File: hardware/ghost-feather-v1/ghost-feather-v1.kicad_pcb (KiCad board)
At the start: 4 copper layers, 106.6 x 106.7 mm, 96 parts, among them J1 Conn_ARM_SWD_TagConnect_TC2030, J2 USB_C_Receptacle_USB2.0, J3 Conn_01x03, J4 Conn_01x03, J5 Conn_01x03, J6 Conn_01x03, J7 Conn_01x08, J8 Conn_01x02, Q1 BSS138, Q2 BSS138, Q3 BSS138, Q4 BSS138, SW2 BOOT0, U1 STM32F722RETx, U2 BMI270, U3 USBLC6-2SC6_MOD, U4 MPM3610, U5 MPM3610, X1 16MHz, X2 32kHz768

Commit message: feat: Via stiching #2
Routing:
- net GND: vias 329 -> 816

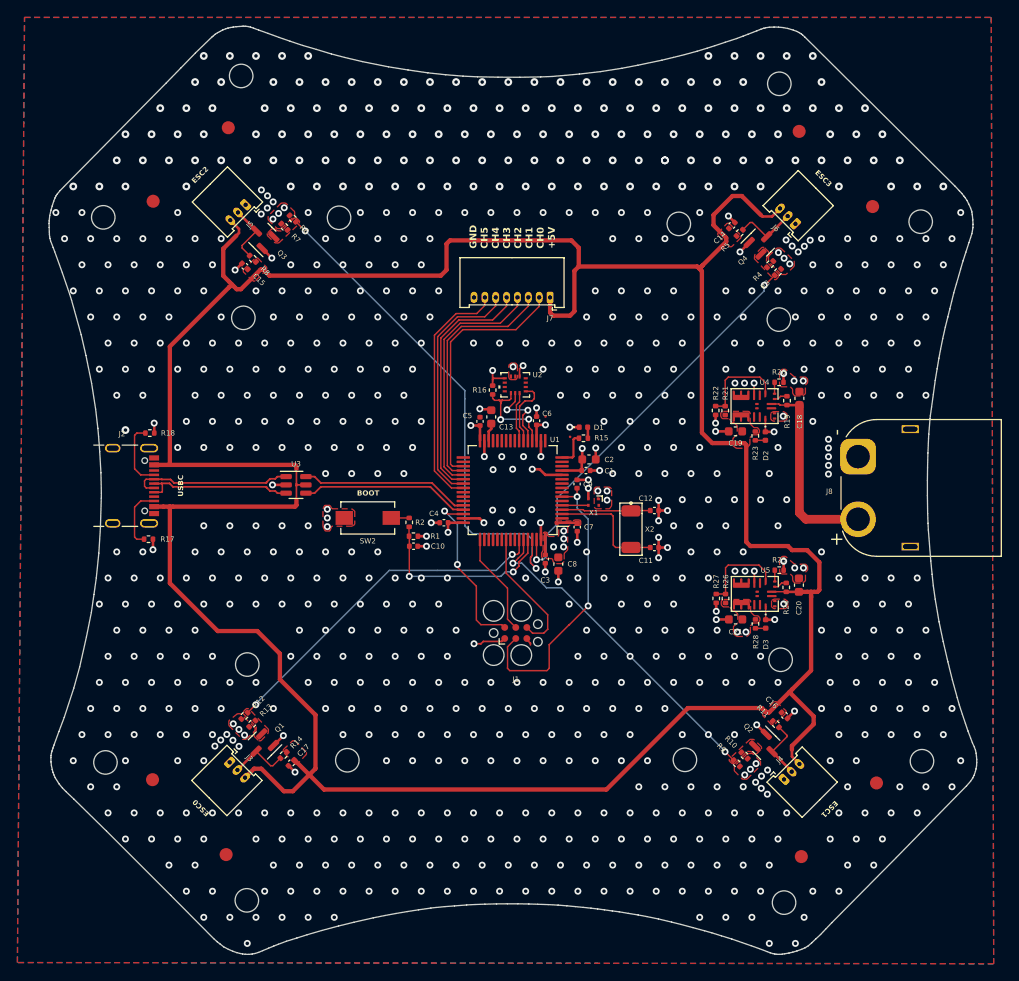
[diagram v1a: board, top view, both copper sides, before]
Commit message: feat: Remove errors and warnings
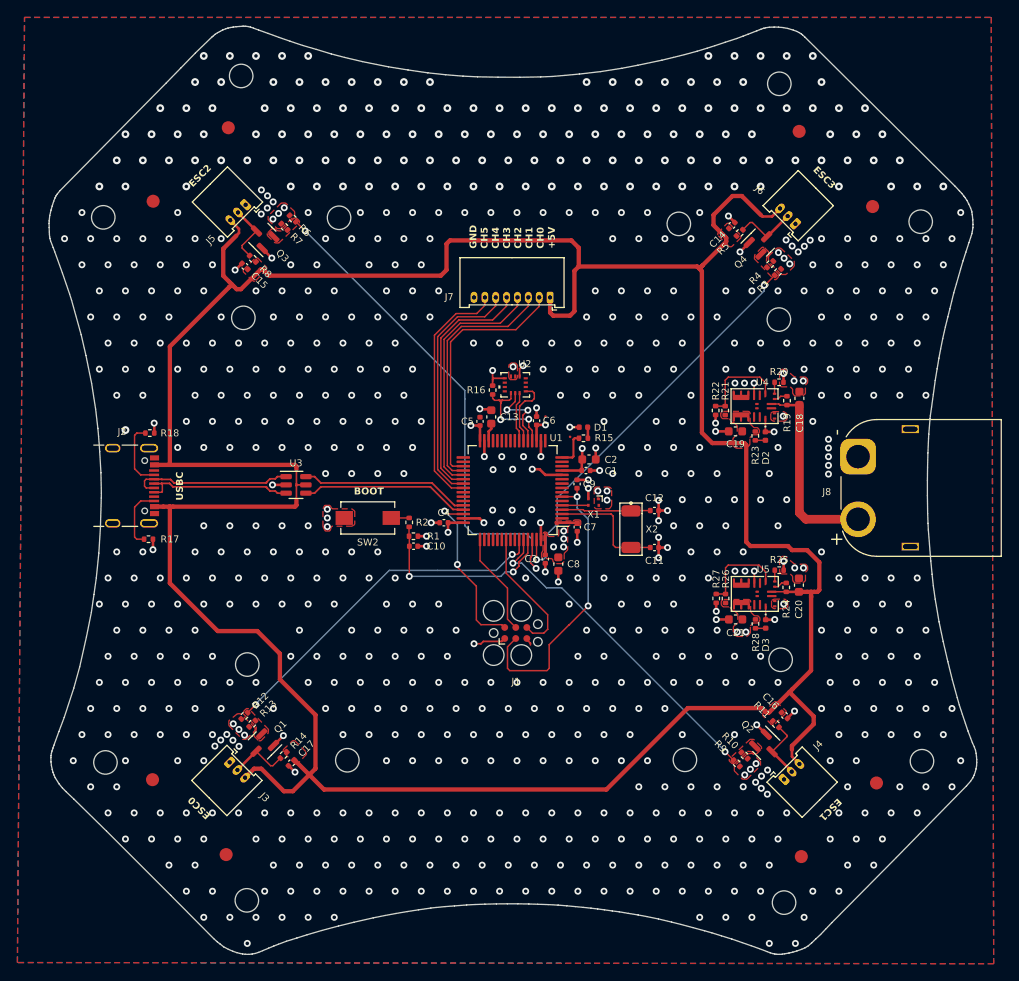
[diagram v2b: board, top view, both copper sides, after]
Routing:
- net GND: vias 816 -> 792

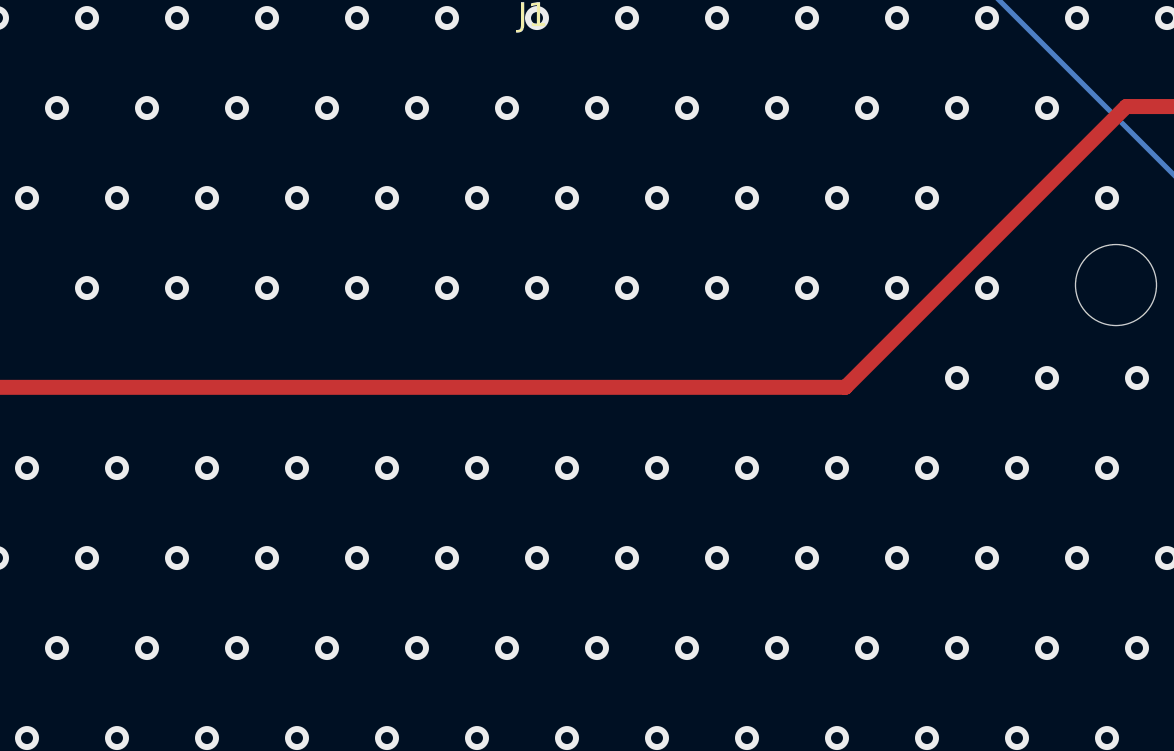
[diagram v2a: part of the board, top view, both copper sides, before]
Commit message: feat: Add silkscreen logo and board name
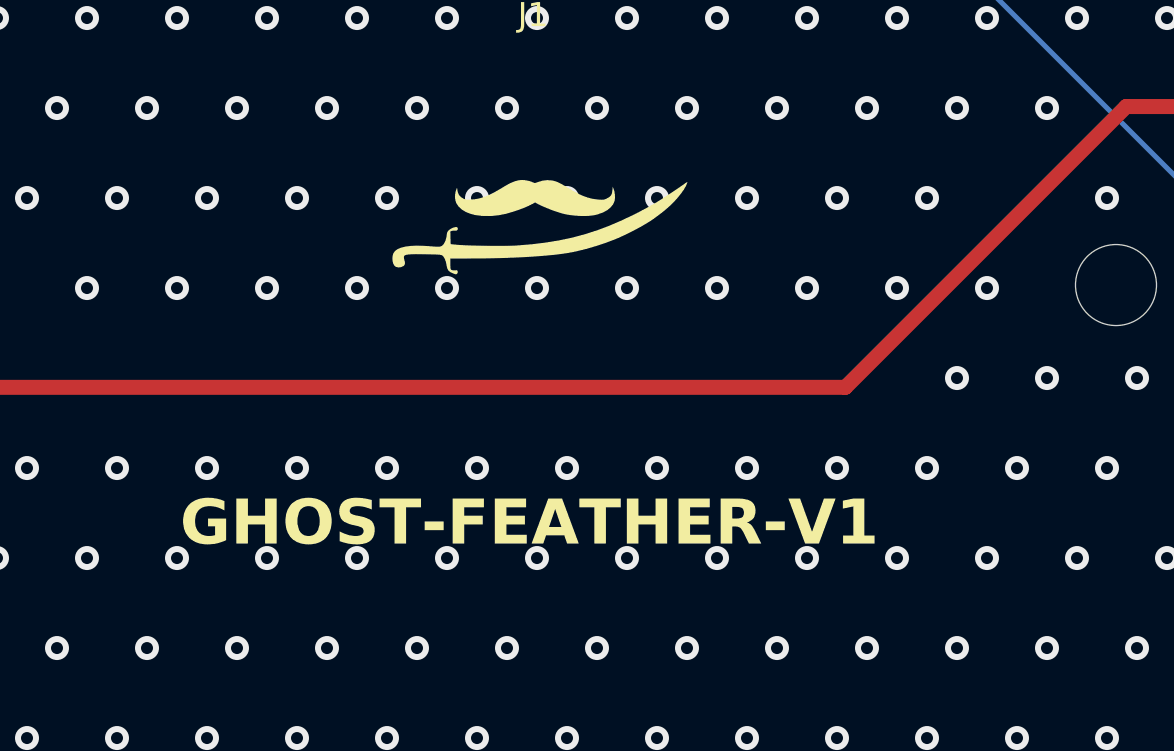
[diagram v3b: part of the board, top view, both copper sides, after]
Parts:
- added G***: LOGO, icons:sabre-with-moustache, F.Cu at (143.1, 120.7)
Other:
- board text added: "GHOST-FEATHER-V1"
